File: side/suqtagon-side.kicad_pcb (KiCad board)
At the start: 2 copper layers, 50.5 x 12.6 mm, 8 parts

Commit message: more advances in side board
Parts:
- removed the REF** at (133.2, 122.4)
- added REF**: TestPoint_Pad_D2.0mm, TestPoint:TestPoint_Pad_D2.0mm, F.Cu at (116.7, 103.3)
- added REF**: TestPoint_Pad_D2.0mm, TestPoint:TestPoint_Pad_D2.0mm, F.Cu at (119.7, 103.3)
- added REF**: TestPoint_Pad_D2.0mm, TestPoint:TestPoint_Pad_D2.0mm, F.Cu at (129.8, 109.3)
- added REF**: TestPoint_Pad_D2.0mm, TestPoint:TestPoint_Pad_D2.0mm, F.Cu at (132.8, 109.3)
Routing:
- net (no net): track 0.07 -> 37.7 mm
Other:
- outline, holes or cut-outs redrawn

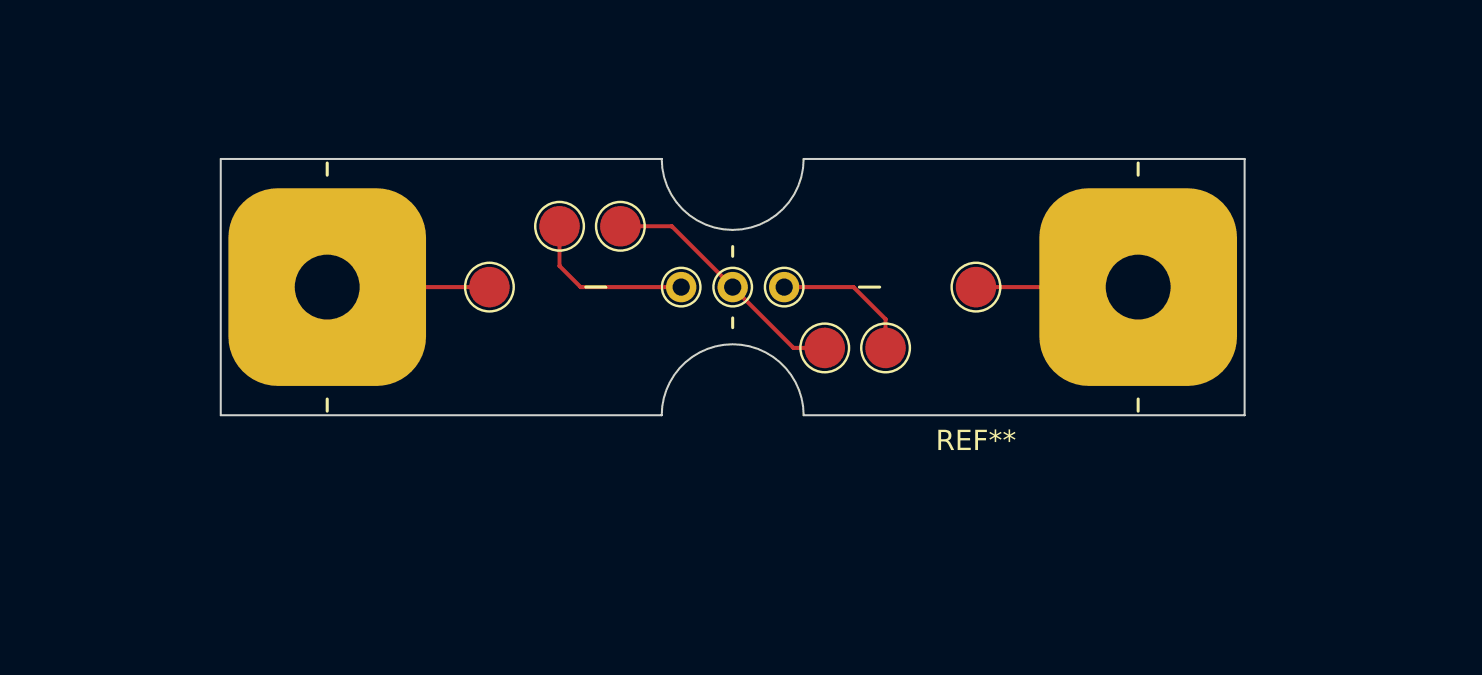
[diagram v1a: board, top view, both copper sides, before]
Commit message: fixing wrong measurements on side pcb
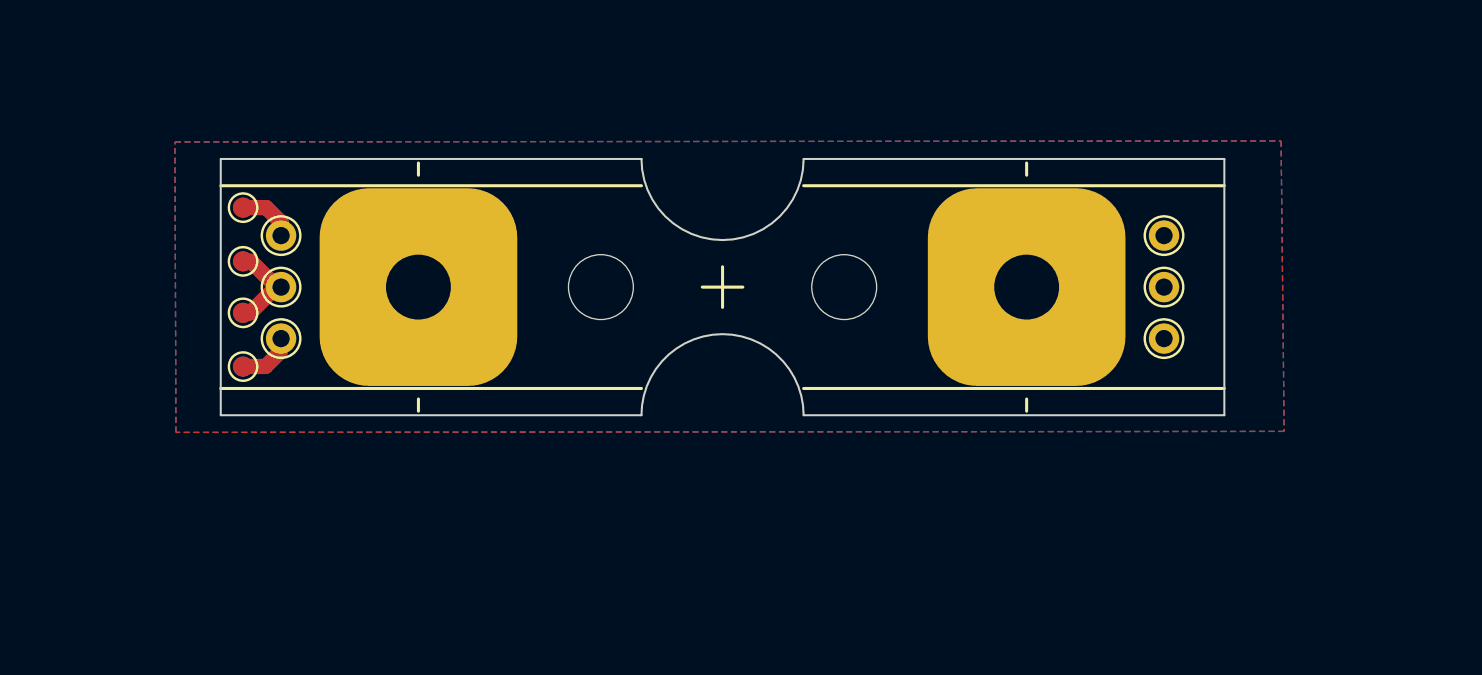
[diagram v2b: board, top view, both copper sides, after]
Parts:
- removed the REF** at (122.7, 106.3)
- removed the REF** at (137.2, 106.3)
- removed the REF** at (116.7, 103.3)
- removed the REF** at (119.7, 103.3)
- removed the REF** at (127.8, 106.3)
- removed the REF** at (129.8, 109.3)
- removed the REF** at (132.8, 109.3)
- removed the REF** at (113.2, 106.3)
- removed the REF** at (125.2, 106.3)
- added REF**: TestPoint_THTPad_D1.5mm_Drill0.7mm, TestPoint:TestPoint_THTPad_D1.5mm_Drill0.7mm, F.Cu at (103.0, 106.3)
- added REF**: TestPoint_THTPad_D1.5mm_Drill0.7mm, TestPoint:TestPoint_THTPad_D1.5mm_Drill0.7mm, F.Cu at (103.0, 108.9)
- added REF**: TestPoint_Pad_D1.0mm, TestPoint:TestPoint_Pad_D1.0mm, F.Cu at (101.1, 105.0)
- added REF**: TestPoint_THTPad_D1.5mm_Drill0.7mm, TestPoint:TestPoint_THTPad_D1.5mm_Drill0.7mm, F.Cu at (146.5, 108.9)
- added REF**: TestPoint_THTPad_D1.5mm_Drill0.7mm, TestPoint:TestPoint_THTPad_D1.5mm_Drill0.7mm, F.Cu at (146.5, 106.3)
- added REF**: TestPoint_Pad_D1.0mm, TestPoint:TestPoint_Pad_D1.0mm, F.Cu at (101.1, 110.2)
- added REF**: TestPoint_THTPad_D1.5mm_Drill0.7mm, TestPoint:TestPoint_THTPad_D1.5mm_Drill0.7mm, F.Cu at (103.0, 103.8)
- added REF**: TestPoint_Pad_D1.0mm, TestPoint:TestPoint_Pad_D1.0mm, F.Cu at (101.1, 102.4)
- added REF**: MountingHole_3.2mm_M3, MountingHole:MountingHole_3.2mm_M3, F.Cu at (130.8, 106.3)
- added REF**: TestPoint_THTPad_D1.5mm_Drill0.7mm, TestPoint:TestPoint_THTPad_D1.5mm_Drill0.7mm, F.Cu at (146.5, 103.8)
- added REF**: TestPoint_Pad_D1.0mm, TestPoint:TestPoint_Pad_D1.0mm, F.Cu at (101.1, 107.6)
- added REF**: MountingHole_3.2mm_M3, MountingHole:MountingHole_3.2mm_M3, F.Cu at (118.8, 106.3)
- moved REF** 5.50 mm to (139.8, 106.3)
- moved REF** 4.50 mm to (109.8, 106.3)
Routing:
- net (no net): track 37.7 -> 10.2 mm
- added copper zone on B.Cu, net (none)
- added copper zone on F.Cu, net (none)
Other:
- board size 50.5 x 12.6 mm -> 49.5 x 12.6 mm

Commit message: all traces routed
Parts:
- added REF**: TestPoint_Pad_D1.0mm, TestPoint:TestPoint_Pad_D1.0mm, F.Cu at (148.4, 110.2)
- added REF**: TestPoint_Pad_D1.0mm, TestPoint:TestPoint_Pad_D1.0mm, F.Cu at (148.4, 105.0)
- added REF**: TestPoint_Pad_D1.0mm, TestPoint:TestPoint_Pad_D1.0mm, F.Cu at (148.4, 102.4)
- added REF**: TestPoint_Pad_D1.0mm, TestPoint:TestPoint_Pad_D1.0mm, F.Cu at (148.4, 107.6)
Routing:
- net (no net): track 10.2 -> 20.3 mm
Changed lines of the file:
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@@
   )
   (net 0 "")
+  (footprint "TestPoint:TestPoint_Pad_D1.0mm" (layer "F.Cu")
+    (at 148.4 110.24)
+    (descr "SMD pad as test Point, diameter 1.0mm")
+    (tags "test point SMD pad")
+    (attr exclude_from_pos_files exclude_from_bom)
+    (fp_text reference "REF**" (at 0 -1.448) (layer "F.SilkS") hide
+      (effects (font (size 1 1) (thickness 0.15)))
+    )
+    (fp_text value "TestPoint_Pad_D1.0mm" (at 0 1.55) (layer "F.Fab")
+      (effects (font (size 1 1) (thickness 0.15)))
+    )
+    (fp_text user "${REFERENCE}" (at 0 -1.45) (layer "F.Fab")
+      (effects (font (size 1 1) (thickness 0.15)))
+    )
+    (fp_circle (center 0 0) (end 0 0.7) (layer "F.SilkS") (width 0.12) (fill none))
+    (fp_circle (center 0 0) (end 1 0) (layer "F.CrtYd") (width 0.05) (fill none))
+    (pad "1" smd circle (at 0 0) (size 1 1) (layers "F.Cu" "F.Mask"))
+  )
   (footprint "TestPoint:TestPoint_THTPad_D1.5mm_Drill0.7mm" (layer "F.Cu")
     (at 102.975 106.32)
@@
   )
   (footprint "TestPoint:TestPoint_Pad_D1.0mm" (layer "F.Cu")
+    (at 148.4 102.4)
+    (descr "SMD pad as test Point, diameter 1.0mm")
+    (tags "test point SMD pad")
+    (attr exclude_from_pos_files exclude_from_bom)
+    (fp_text reference "REF**" (at 0 -1.448) (layer "F.SilkS") hide
+      (effects (font (size 1 1) (thickness 0.15)))
+    )
+    (fp_text value "TestPoint_Pad_D1.0mm" (at 0 1.55) (layer "F.Fab")
+      (effects (font (size 1 1) (thickness 0.15)))
+    )
+    (fp_text user "${REFERENCE}" (at 0 -1.45) (layer "F.Fab")
+      (effects (font (size 1 1) (thickness 0.15)))
+    )
+    (fp_circle (center 0 0) (end 0 0.7) (layer "F.SilkS") (width 0.12) (fill none))
+    (fp_circle (center 0 0) (end 1 0) (layer "F.CrtYd") (width 0.05) (fill none))
+    (pad "1" smd circle (at 0 0) (size 1 1) (layers "F.Cu" "F.Mask"))
+  )
+  (footprint "TestPoint:TestPoint_Pad_D1.0mm" (layer "F.Cu")
+    (at 148.4 107.59)
+    (descr "SMD pad as test Point, diameter 1.0mm")
+    (tags "test point SMD pad")
+    (attr exclude_from_pos_files exclude_from_bom)
+    (fp_text reference "REF**" (at 0 -1.448) (layer "F.SilkS") hide
+      (effects (font (size 1 1) (thickness 0.15)))
+    )
+    (fp_text value "TestPoint_Pad_D1.0mm" (at 0 1.55) (layer "F.Fab")
+      (effects (font (size 1 1) (thickness 0.15)))
+    )
+    (fp_text user "${REFERENCE}" (at 0 -1.45) (layer "F.Fab")
+      (effects (font (size 1 1) (thickness 0.15)))
+    )
+    (fp_circle (center 0 0) (end 0 0.7) (layer "F.SilkS") (width 0.12) (fill none))
+    (fp_circle (center 0 0) (end 1 0) (layer "F.CrtYd") (width 0.05) (fill none))
+    (pad "1" smd circle (at 0 0) (size 1 1) (layers "F.Cu" "F.Mask"))
+  )
+  (footprint "TestPoint:TestPoint_Pad_D1.0mm" (layer "F.Cu")
     (at 101.1 110.24)
     (descr "SMD pad as test Point, diameter 1.0mm")
@@
   )
   (footprint "TestPoint:TestPoint_Pad_D1.0mm" (layer "F.Cu")
+    (at 148.4 105.05)
+    (descr "SMD pad as test Point, diameter 1.0mm")
+    (tags "test point SMD pad")
+    (attr exclude_from_pos_files exclude_from_bom)
+    (fp_text reference "REF**" (at 0 -1.448) (layer "F.SilkS") hide
+      (effects (font (size 1 1) (thickness 0.15)))
+    )
+    (fp_text value "TestPoint_Pad_D1.0mm" (at 0 1.55) (layer "F.Fab")
+      (effects (font (size 1 1) (thickness 0.15)))
+    )
+    (fp_text user "${REFERENCE}" (at 0 -1.45) (layer "F.Fab")
+      (effects (font (size 1 1) (thickness 0.15)))
+    )
+    (fp_circle (center 0 0) (end 0 0.7) (layer "F.SilkS") (width 0.12) (fill none))
+    (fp_circle (center 0 0) (end 1 0) (layer "F.CrtYd") (width 0.05) (fill none))
+    (pad "1" smd circle (at 0 0) (size 1 1) (layers "F.Cu" "F.Mask"))
+  )
+  (footprint "TestPoint:TestPoint_Pad_D1.0mm" (layer "F.Cu")
     (at 101.1 105.05)
     (descr "SMD pad as test Point, diameter 1.0mm")
@@
     (pad "1" thru_hole circle (at 0 0) (size 1.5 1.5) (drill 0.85) (layers *.Cu *.Mask))
   )
-  (gr_line (start 100.631 119.5832) (end 122.381 119.5832) (layer "B.SilkS") (width 2))
-  (gr_line (start 129.079 94.3864) (end 150.829 94.3864) (layer "B.SilkS") (width 2))
-  (gr_line (start 164.3888 109.1552) (end 164.3888 98.5152) (layer "B.SilkS") (width 2))
-  (gr_line (start 92.3036 111.64) (end 92.3036 101) (layer "B.SilkS") (width 2))
-  (gr_line (start 100.2246 94.2848) (end 121.9746 94.2848) (layer "B.SilkS") (width 2))
-  (gr_line (start 129.2822 116.6368) (end 151.0322 116.6368) (layer "B.SilkS") (width 2))
+  (gr_line (start 100.631 119.5832) (end 122.381 119.5832) (layer "B.SilkS") (width 1.5))
+  (gr_line (start 129.079 94.3864) (end 150.829 94.3864) (layer "B.SilkS") (width 1.5))
+  (gr_line (start 164.3888 109.1552) (end 164.3888 98.5152) (layer "B.SilkS") (width 1.5))
+  (gr_line (start 92.3036 111.64) (end 92.3036 101) (layer "B.SilkS") (width 1.5))
+  (gr_line (start 100.2246 94.2848) (end 121.9746 94.2848) (layer "B.SilkS") (width 1.5))
+  (gr_line (start 129.2822 116.6368) (end 151.0322 116.6368) (layer "B.SilkS") (width 1.5))
   (gr_line (start 139.75 111.84) (end 139.75 112.44) (layer "F.SilkS") (width 0.15))
   (gr_line (start 100 111.32) (end 120.75 111.32) (layer "F.SilkS") (width 0.15))
@@
   (gr_line (start 100 100) (end 100 112.64) (layer "Edge.Cuts") (width 0.1))
   (segment (start 101.1 107.59) (end 101.4515 107.59) (width 0.75) (layer "F.Cu") (net 0))
+  (segment (start 146.558 106.2736) (end 146.9136 106.2736) (width 0.75) (layer "F.Cu") (net 0))
   (segment (start 101.4515 107.59) (end 102.7215 106.32) (width 0.75) (layer "F.Cu") (net 0))
+  (segment (start 147.282 102.4) (end 148.3868 102.4) (width 0.75) (layer "F.Cu") (net 0))
   (segment (start 101.2444 110.236) (end 102.2096 110.236) (width 0.75) (layer "F.Cu") (net 0))
+  (segment (start 148.3868 102.4) (end 148.4 102.4) (width 0.2) (layer "F.Cu") (net 0))
   (segment (start 102.9208 109.5248) (end 102.9208 108.8136) (width 0.75) (layer "F.Cu") (net 0))
+  (segment (start 146.525 103.157) (end 147.282 102.4) (width 0.75) (layer "F.Cu") (net 0))
   (segment (start 102.2476 102.4) (end 102.975 103.1274) (width 0.75) (layer "F.Cu") (net 0))
-  (segment (start 108.3608 106.32) (end 108.3564 106.3244) (width 0.2) (layer "F.Cu") (net 0))
+  (segment (start 146.525 106.32) (end 146.8076 106.32) (width 0.75) (layer "F.Cu") (net 0))
   (segment (start 101.1936 102.4) (end 102.2476 102.4) (width 0.75) (layer "F.Cu") (net 0))
   (segment (start 102.2096 110.236) (end 102.9208 109.5248) (width 0.75) (layer "F.Cu") (net 0))
-  (segment (start 142.0324 106.32) (end 142.0368 106.3244) (width 0.2) (layer "F.Cu") (net 0))
+  (segment (start 146.8076 106.32) (end 148.0776 107.59) (width 0.75) (layer "F.Cu") (net 0))
   (segment (start 102.975 103.1274) (end 102.975 103.78) (width 0.75) (layer "F.Cu") (net 0))
+  (segment (start 146.9136 106.2736) (end 148.1372 105.05) (width 0.75) (layer "F.Cu") (net 0))
   (segment (start 101.494 105.05) (end 102.764 106.32) (width 0.75) (layer "F.Cu") (net 0))
+  (segment (start 146.525 103.78) (end 146.525 103.157) (width 0.75) (layer "F.Cu") (net 0))
+  (segment (start 146.525 109.3902) (end 147.3748 110.24) (width 0.75) (layer "F.Cu") (net 0))
+  (segment (start 148.336 107.59) (end 148.4 107.59) (width 0.2) (layer "F.Cu") (net 0))
+  (segment (start 148.1372 105.05) (end 148.4 105.05) (width 0.2) (layer "F.Cu") (net 0))
   (segment (start 102.7215 106.32) (end 102.975 106.32) (width 0.75) (layer "F.Cu") (net 0))
+  (segment (start 147.3748 110.24) (end 148.1836 110.24) (width 0.75) (layer "F.Cu") (net 0))
   (segment (start 102.764 106.32) (end 102.975 106.32) (width 0.75) (layer "F.Cu") (net 0))
+  (segment (start 148.0776 107.59) (end 148.336 107.59) (width 0.75) (layer "F.Cu") (net 0))
+  (segment (start 146.525 108.86) (end 146.525 109.3902) (width 0.75) (layer "F.Cu") (net 0))
   (segment (start 101.1 105.05) (end 101.494 105.05) (width 0.75) (layer "F.Cu") (net 0))
   (zone (net 0) (net_name "") (layers F&B.Cu) (hatch edge 0.508)
